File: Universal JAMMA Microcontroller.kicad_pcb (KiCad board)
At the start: 2 copper layers, 111 x 78.8 mm, 43 parts, among them U1 LM386, U2 74LS86, U3 MC34063AP, U4 328P

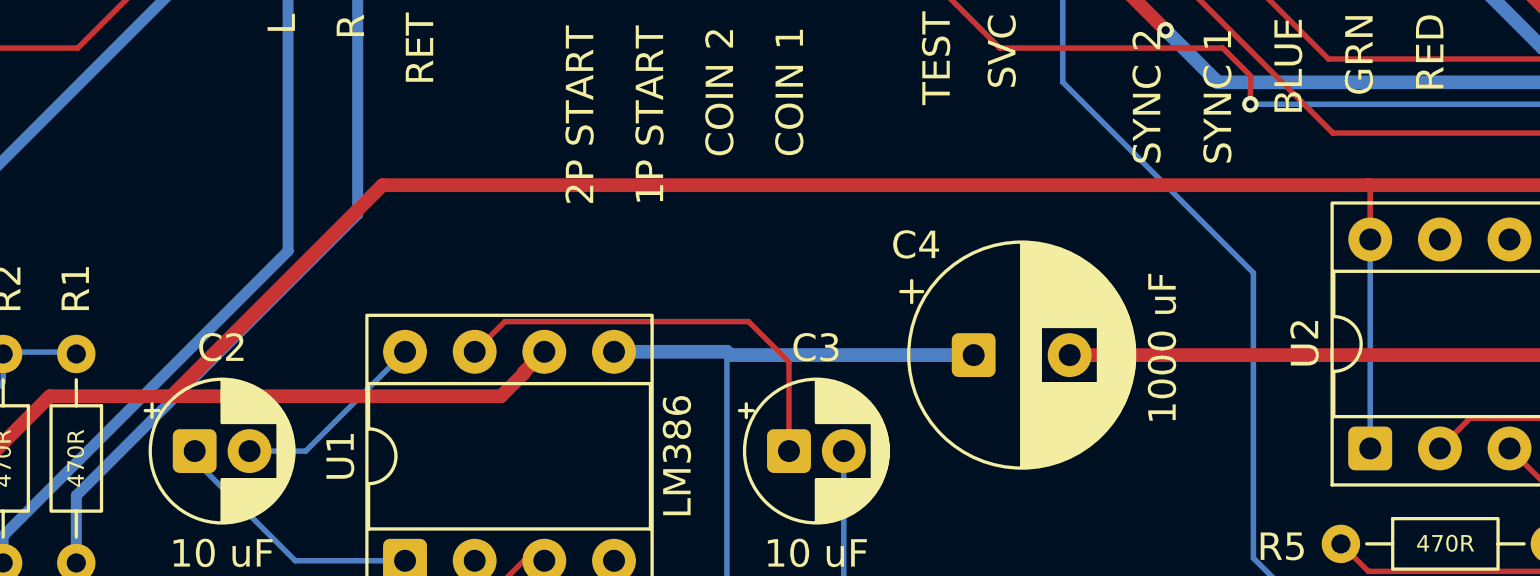
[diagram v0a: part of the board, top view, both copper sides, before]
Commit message: clear a red path to pins
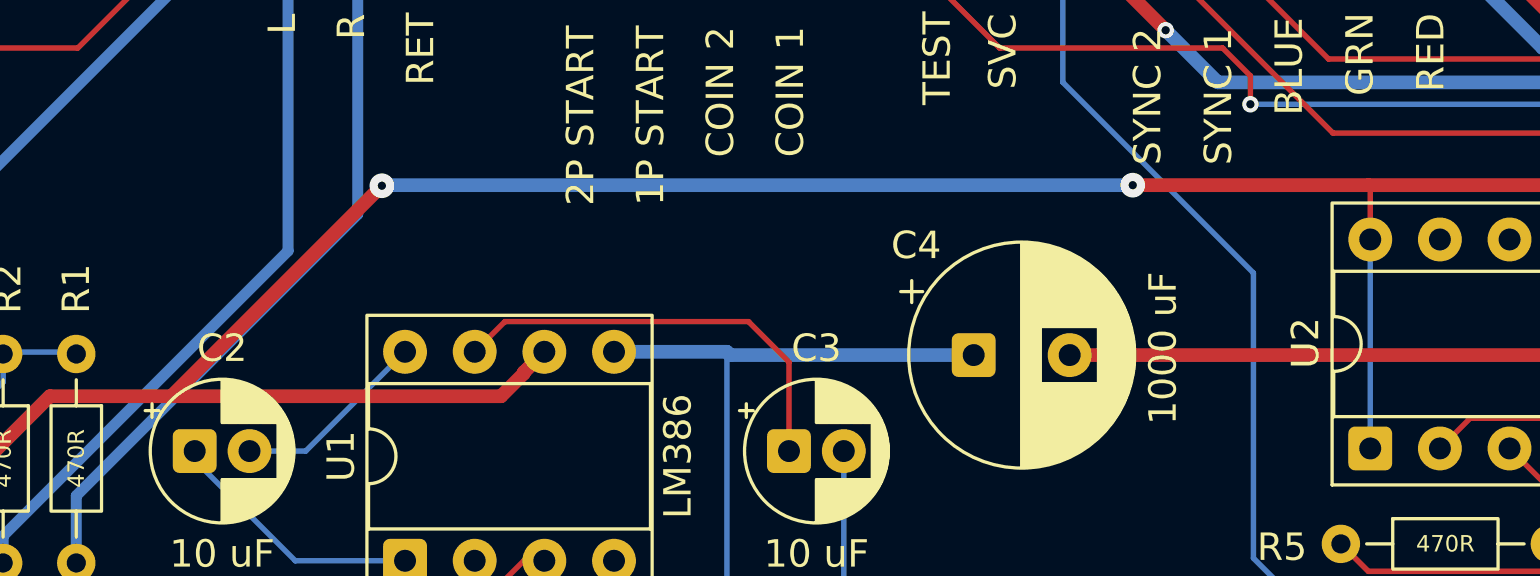
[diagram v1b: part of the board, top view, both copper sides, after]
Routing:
- net +5V: vias 5 -> 7
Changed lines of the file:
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@@
 	(segment
 		(start 135.441406 101)
-		(end 127.745851 108.695555)
+		(end 135.420703 101.020703)
 		(width 0.5)
 		(layer "F.Cu")
@@
 	(segment
 		(start 171.4 101)
-		(end 135.441406 101)
+		(end 162.8 101)
 		(width 0.5)
 		(layer "F.Cu")
@@
 		(end 195.033352 69.245852)
 		(width 2.5)
+		(layer "F.Cu")
+		(net 2)
+	)
+	(segment
+		(start 135.420703 101.020703)
+		(end 127.745851 108.695555)
+		(width 0.5)
 		(layer "F.Cu")
 		(net 2)
@@
 	)
 	(via
+		(at 162.8 101)
+		(size 0.9)
+		(drill 0.3)
+		(layers "F.Cu" "B.Cu")
+		(net 2)
+	)
+	(via
 		(at 137.2 138.2)
 		(size 0.9)
@@
 		(net 2)
 	)
+	(via
+		(at 135.420703 101.020703)
+		(size 0.9)
+		(drill 0.3)
+		(layers "F.Cu" "B.Cu")
+		(net 2)
+	)
 	(segment
 		(start 195.03 75.83677)
@@
 		(layer "B.Cu")
 		(net 2)
+	)
+	(segment
+		(start 162.8 101)
+		(end 135.441406 101)
+		(width 0.5)
+		(layer "B.Cu")
+		(net 2)

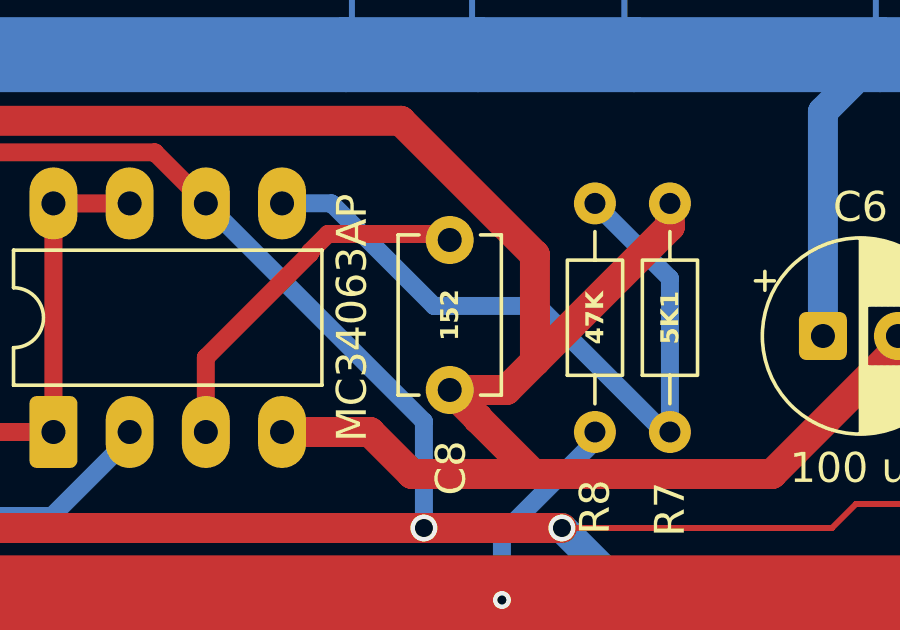
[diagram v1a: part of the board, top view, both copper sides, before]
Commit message: 152 becomes 2A152J (reduces noise)
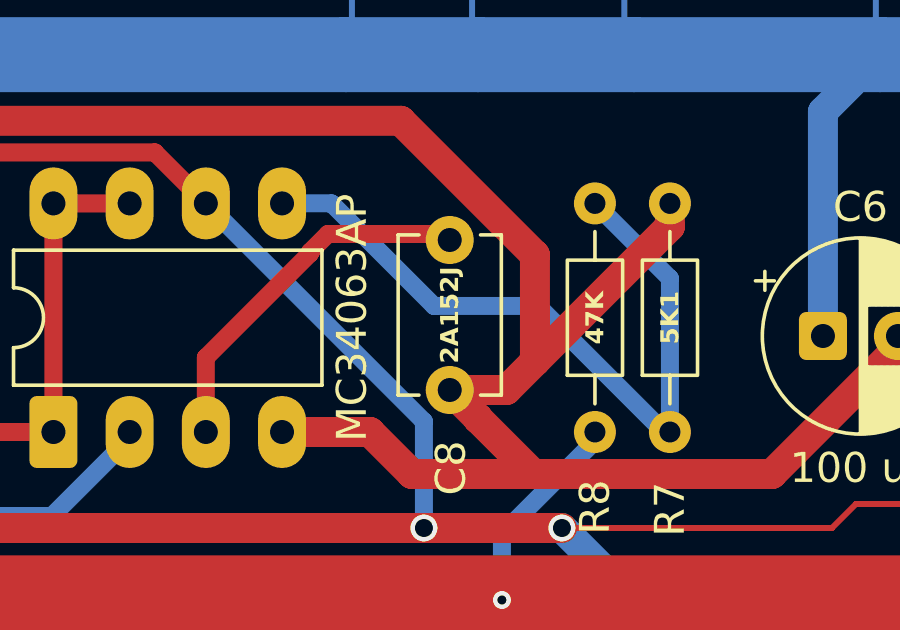
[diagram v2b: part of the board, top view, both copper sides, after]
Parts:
- C8: value 152 -> 2A152J
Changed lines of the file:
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@@
 			)
 		)
-		(property "Value" "152"
+		(property "Value" "2A152J"
 			(at 2.5 0 90)
 			(layer "F.SilkS")
